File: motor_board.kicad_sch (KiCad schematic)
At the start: 44 parts, among them J1 MyRIO_C, J10 ESCON_24-2, J11 Conn_01x02, J12 Conn_01x05, J13 Conn_01x03, J14 BNC, J15 BNC, J2 BNC, J3 BNC, J4 BNC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

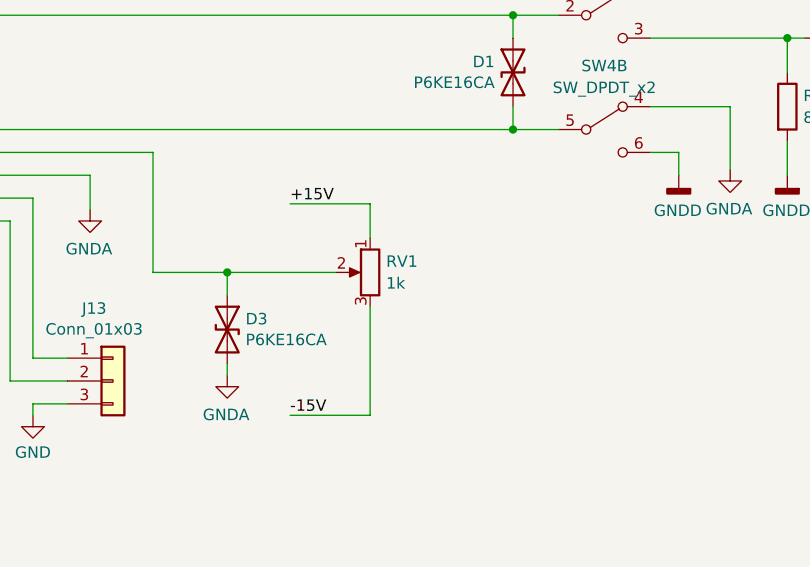
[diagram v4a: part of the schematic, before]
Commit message: updated the board to use a 10k pot that is hopefully more heat resistant and has longer leads.
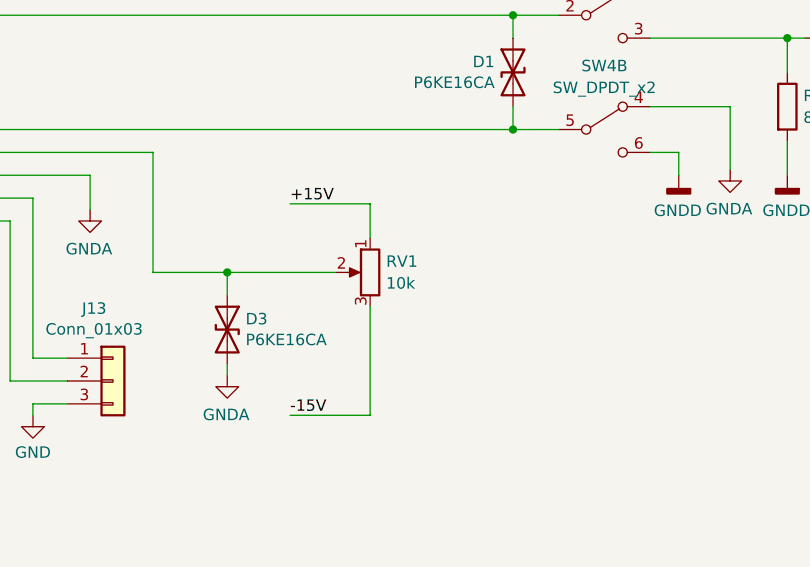
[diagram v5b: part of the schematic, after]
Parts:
- RV1: value 1k -> 10k; footprint motor_board:CUI PTN06-E Pot -> Potentiometer_THT:Potentiometer_Piher_PT-10-V10_Vertical; DigiKey P/N 2223-PTN06-E01CB20-ND -> 1993-1116-ND
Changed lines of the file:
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@@
       (effects (font (size 1.27 1.27)) (justify right))
     )
-    (property "Value" "1k" (at 110.998 107.8921 0)
+    (property "Value" "10k" (at 110.998 107.8921 0)
       (effects (font (size 1.27 1.27)) (justify right))
     )
-    (property "Footprint" "motor_board:CUI PTN06-E Pot" (at 109.22 106.68 0)
+    (property "Footprint" "Potentiometer_THT:Potentiometer_Piher_PT-10-V10_Vertical" (at 109.22 106.68 0)
       (effects (font (size 1.27 1.27)) hide)
     )
@@
       (effects (font (size 1.27 1.27)) hide)
     )
-    (property "DigiKey P/N" "2223-PTN06-E01CB20-ND" (at 109.22 106.68 0)
+    (property "DigiKey P/N" "1993-1116-ND" (at 109.22 106.68 0)
       (effects (font (size 1.27 1.27)) hide)
     )

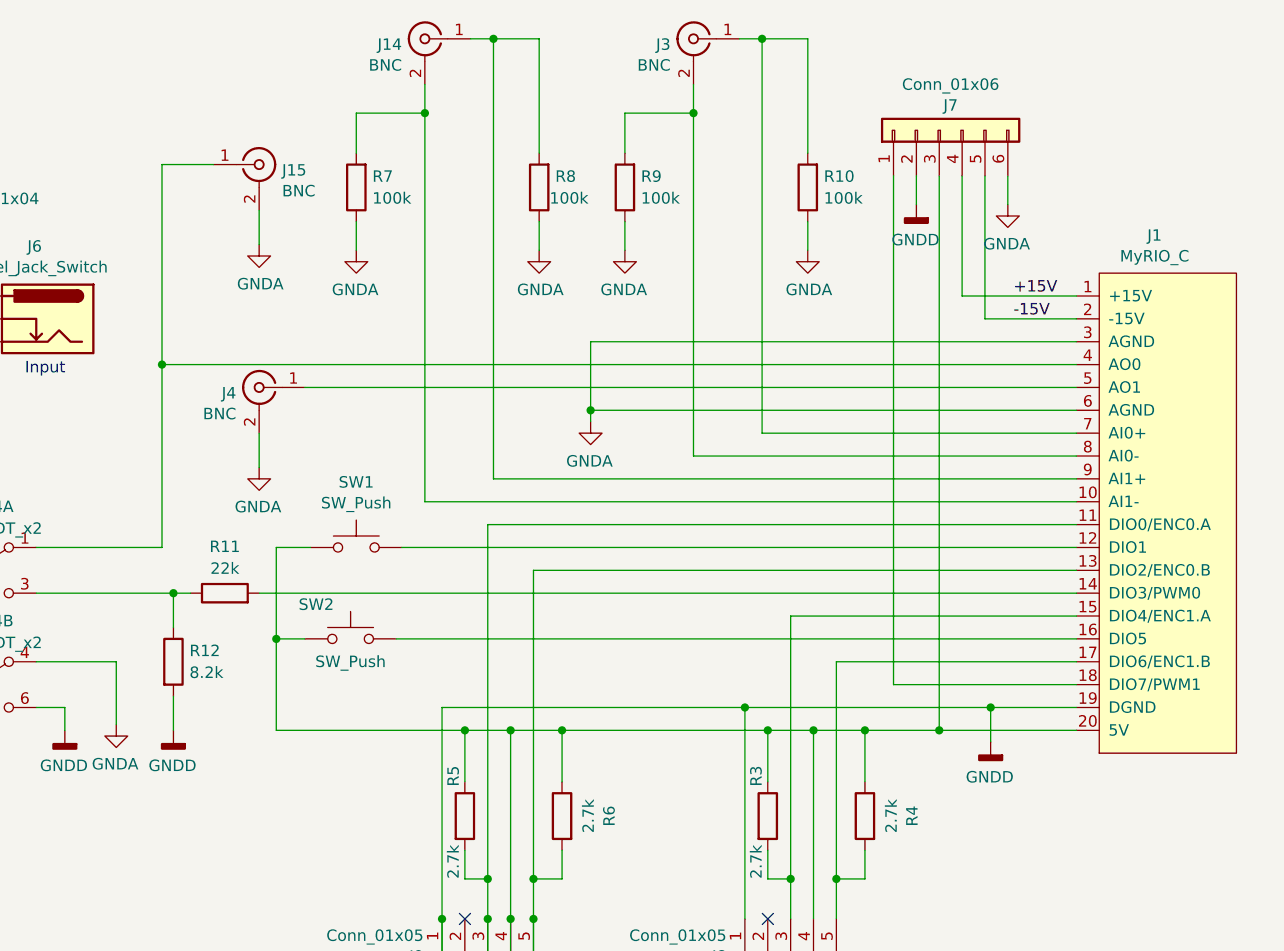
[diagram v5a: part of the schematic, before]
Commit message: added a resistor divider to get the correct current for lab 4, added DIO3 to the aux header, and changed to a more durable 10 k put to keep from overloading the +/-15 V supply.
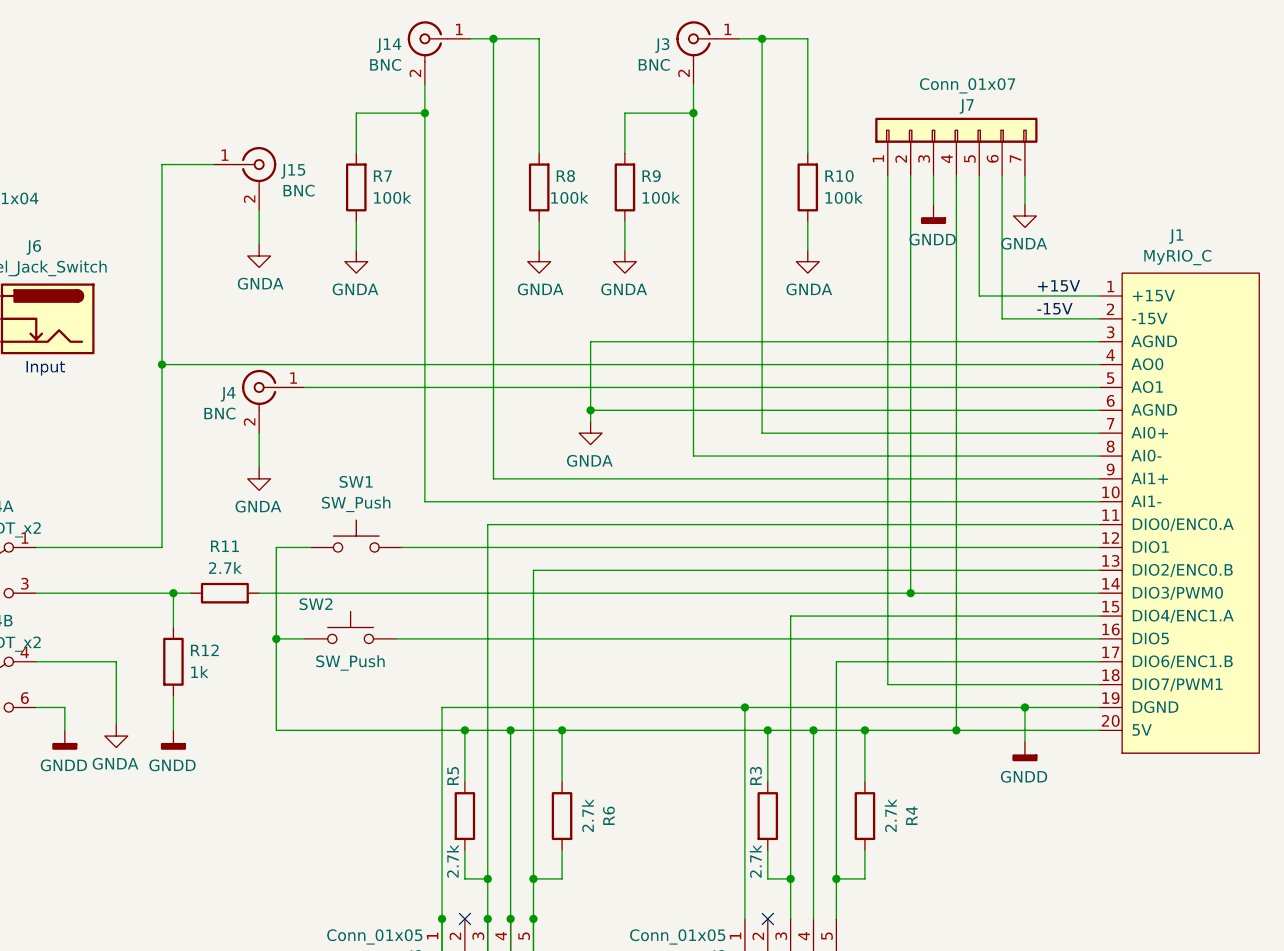
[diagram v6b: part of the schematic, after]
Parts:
- J7: value Conn_01x06 -> Conn_01x07; footprint Connector_PinSocket_2.54mm:PinSocket_1x06_P2.54mm_Vertical -> Connector_PinSocket_2.54mm:PinSocket_1x07_P2.54mm_Vertical; symbol Connector_Generic:Conn_01x06 -> Connector_Generic:Conn_01x07; DigiKey P/N S7004-ND -> S7005-ND
- R11: value 22k -> 2.7k; DigiKey P/N 13-MFR-12FTF52-22KCT-ND -> 13-MFR-12FTF52-2K7CT-ND
- R12: value 8.2k -> 1k; DigiKey P/N 13-MFR-12FTF52-8K2CT-ND -> 13-MFR-12FTF52-1KCT-ND
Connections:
- net +15V: now also J7.5 (Pin_5); no longer J7.4 (Pin_4)
- net -15V: now also J7.6 (Pin_6); no longer J7.5 (Pin_5)
- net GNDA: now also J7.7 (Pin_7); no longer J7.6 (Pin_6)
- net GNDD: now also J7.3 (Pin_3); no longer J7.2 (Pin_2)
- net at J1.14 (DIO3/PWM0), R11.2: now also J7.2 (Pin_2)
- net at J1.20 (5V), J12.4 (Pin_4), J8.4 (Pin_4)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: now also J7.4 (Pin_4); no longer J7.3 (Pin_3)
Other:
- moved on the sheet: J1

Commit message: The final design
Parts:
- C1: footprint Resistor_THT:R_Axial_DIN0204_L3.6mm_D1.6mm_P5.08mm_Horizontal -> Capacitor_THT:CP_Radial_D8.0mm_P3.50mm
- R11: value 2.7k -> 12k; DigiKey P/N 13-MFR-12FTF52-2K7CT-ND -> 13-MFR-12FTF52-12KCT-ND
- R12: value 1k -> 4.7k; DigiKey P/N 13-MFR-12FTF52-1KCT-ND -> 13-MFR-12FTF52-4K7CT-ND
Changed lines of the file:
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@@
       (effects (font (size 1.27 1.27)) (justify left))
     )
-    (property "Footprint" "Resistor_THT:R_Axial_DIN0204_L3.6mm_D1.6mm_P5.08mm_Horizontal" (at 98.7298 57.785 0)
+    (property "Footprint" "Capacitor_THT:CP_Radial_D8.0mm_P3.50mm" (at 98.7298 57.785 0)
       (effects (font (size 1.27 1.27)) hide)
     )
@@
       (effects (font (size 1.27 1.27)) (justify left))
     )
-    (property "Value" "1k" (at 157.353 89.4771 0)
+    (property "Value" "4.7k" (at 157.353 89.4771 0)
       (effects (font (size 1.27 1.27)) (justify left))
     )
@@
       (effects (font (size 1.27 1.27)) hide)
     )
-    (property "DigiKey P/N" "13-MFR-12FTF52-1KCT-ND" (at 155.575 88.265 0)
+    (property "DigiKey P/N" "13-MFR-12FTF52-4K7CT-ND" (at 155.575 88.265 0)
       (effects (font (size 1.27 1.27)) hide)
     )
@@
       (effects (font (size 1.27 1.27)))
     )
-    (property "Value" "2.7k" (at 161.29 77.9089 90)
+    (property "Value" "12k" (at 161.29 77.9089 90)
       (effects (font (size 1.27 1.27)))
     )
@@
       (effects (font (size 1.27 1.27)) hide)
     )
-    (property "DigiKey P/N" "13-MFR-12FTF52-2K7CT-ND" (at 161.29 80.645 0)
-      (effects (font (size 1.27 1.27)) hide)
-    )
+    (property "DigiKey P/N" "13-MFR-12FTF52-12KCT-ND" (at 161.29 80.645 0)
+      (effects (font (size 1.27 1.27)) hide)
+    )
